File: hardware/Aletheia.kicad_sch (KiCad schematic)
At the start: 29 parts, among them J101 Conn_01x04, SW101 SW_DIP_x08, SW102 SW_DIP_x08, SW104 SW_DIP_x04, SW105 G19AP, U101 W65C02S6TPG-14, U102 AS6C1008-55PCN, U103 W65C22N6TPG-14, U104 74LS04, U105 74LS08, U106 74LS21, Y101 ECS-100AX-010

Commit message: Update design files to reflect new name
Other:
- company: (none) -> Finite Devices
- title: (none) -> Alethia

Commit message: Fix typo in branding files
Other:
- title: Alethia -> Aletheia

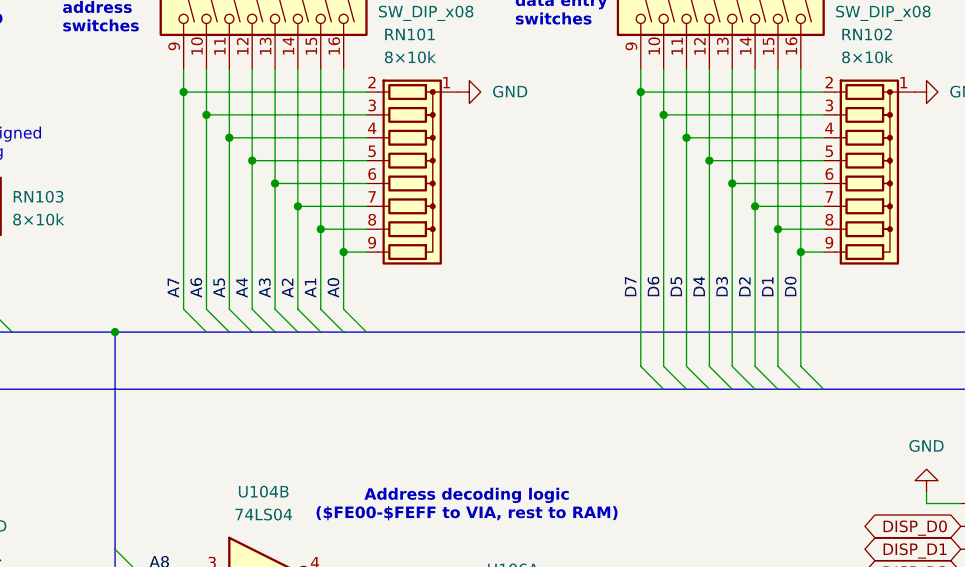
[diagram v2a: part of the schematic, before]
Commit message: Fix order of DIP switch lines in hardware
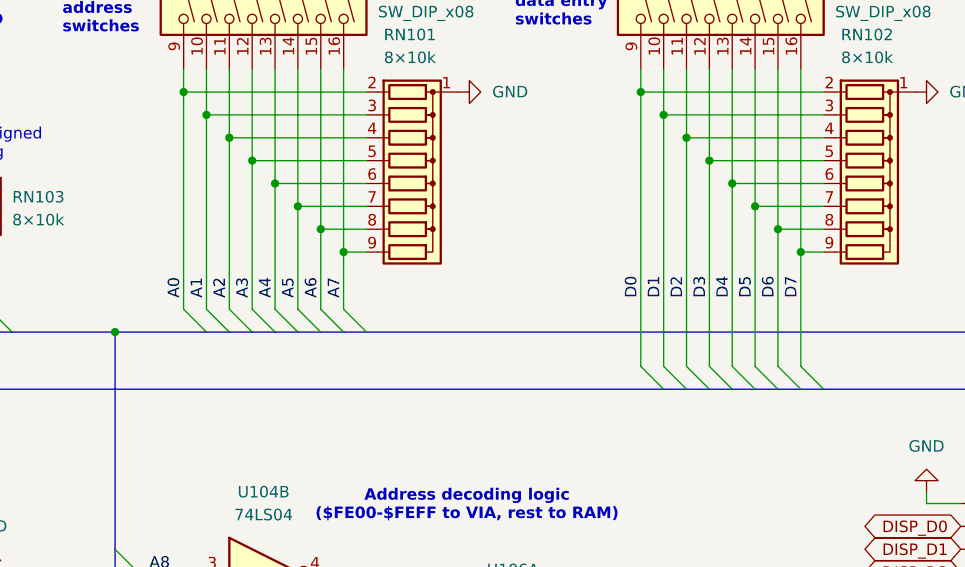
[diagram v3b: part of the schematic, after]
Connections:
- net A0: now also RN101.2 (R1), SW101.9; no longer RN101.9 (R8), SW101.16
- net A1: now also RN101.3 (R2), SW101.10; no longer RN101.8 (R7), SW101.15
- net A2: now also RN101.4 (R3), SW101.11; no longer RN101.7 (R6), SW101.14
- net A3: now also RN101.5 (R4), SW101.12; no longer RN101.6 (R5), SW101.13
- net A4: now also RN101.6 (R5), SW101.13; no longer RN101.5 (R4), SW101.12
- net A5: now also RN101.7 (R6), SW101.14; no longer RN101.4 (R3), SW101.11
- net A6: now also RN101.8 (R7), SW101.15; no longer RN101.3 (R2), SW101.10
- net A7: now also RN101.9 (R8), SW101.16; no longer RN101.2 (R1), SW101.9
- net D0: now also RN102.2 (R1), SW102.9; no longer RN102.9 (R8), SW102.16
- net D1: now also RN102.3 (R2), SW102.10; no longer RN102.8 (R7), SW102.15
- net D2: now also RN102.4 (R3), SW102.11; no longer RN102.7 (R6), SW102.14
- net D3: now also RN102.5 (R4), SW102.12; no longer RN102.6 (R5), SW102.13
- net D4: now also RN102.6 (R5), SW102.13; no longer RN102.5 (R4), SW102.12
- net D5: now also RN102.7 (R6), SW102.14; no longer RN102.4 (R3), SW102.11
- net D6: now also RN102.8 (R7), SW102.15; no longer RN102.3 (R2), SW102.10
- net D7: now also RN102.9 (R8), SW102.16; no longer RN102.2 (R1), SW102.9
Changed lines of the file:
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@@
 		)
 	)
-	(label "A5"
+	(label "A2"
 		(at 133.35 83.82 90)
 		(effects
@@
 		)
 	)
-	(label "A2"
+	(label "A5"
 		(at 140.97 83.82 90)
 		(effects
@@
 		)
 	)
-	(label "D0"
+	(label "D7"
 		(at 196.85 83.82 90)
 		(effects
@@
 		)
 	)
-	(label "D6"
+	(label "D1"
 		(at 181.61 83.82 90)
 		(effects
@@
 		)
 	)
-	(label "D7"
+	(label "D0"
 		(at 179.07 83.82 90)
 		(effects
@@
 		)
 	)
-	(label "D4"
+	(label "D3"
 		(at 186.69 83.82 90)
 		(effects
@@
 		)
 	)
-	(label "A0"
+	(label "A7"
 		(at 146.05 83.82 90)
 		(effects
@@
 		)
 	)
-	(label "A7"
+	(label "A0"
 		(at 128.27 83.82 90)
 		(effects
@@
 		)
 	)
-	(label "A1"
+	(label "A6"
 		(at 143.51 83.82 90)
 		(effects
@@
 		)
 	)
-	(label "A3"
+	(label "A4"
 		(at 138.43 83.82 90)
 		(effects
@@
 		)
 	)
-	(label "A4"
+	(label "A3"
 		(at 135.89 83.82 90)
 		(effects
@@
 		)
 	)
-	(label "D5"
+	(label "D2"
 		(at 184.15 83.82 90)
 		(effects
@@
 		)
 	)
-	(label "D3"
+	(label "D4"
 		(at 189.23 83.82 90)
 		(effects
@@
 		)
 	)
-	(label "D1"
+	(label "D6"
 		(at 194.31 83.82 90)
 		(effects
@@
 		)
 	)
-	(label "D2"
+	(label "D5"
 		(at 191.77 83.82 90)
 		(effects
@@
 		)
 	)
-	(label "A6"
+	(label "A1"
 		(at 130.81 83.82 90)
 		(effects
